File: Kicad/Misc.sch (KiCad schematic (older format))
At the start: 34 parts, among them IC1 DS1233-10+, J1 Data Bus Pin Header, J2 Address Bus Pin Header, J3 uSeq Pin Header, SW1 SW_Push, U21 74HCT139, U26 ECS-100AX-035

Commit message: Added the equ pseudo-op. Rearranged the PCB layout.
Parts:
- removed C24: 0.1uF, Capacitor_SMD:C_0603_1608Metric_Pad1.05x0.95mm_HandSolder, symbol Device:C_Small
- added J4: Control Lines Pin Header, Connector_PinSocket_2.54mm:PinSocket_1x18_P2.54mm_Vertical, symbol Connector:Conn_01x18_Female
- added J5: Clock Pin Header, Connector_PinSocket_2.54mm:PinSocket_1x02_P2.54mm_Vertical, symbol Connector:Conn_01x02_Female
- U21: footprint Package_SO:SOIC-16W_5.3x10.2mm_P1.27mm -> Package_SO:SOIC-16_3.9x9.9mm_P1.27mm
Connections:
- net Clk: now also J5.1 (Pin_1)
- net GND: now also J4.1 (Pin_1), J5.2 (Pin_2)
- net VCC: now also J1.9 (Pin_9), J2.17 (Pin_17), J3.5 (Pin_5), J4.2 (Pin_2)
- new net ALUop0: J4.3 (Pin_3)
- new net ALUop1: J4.4 (Pin_4)
- new net ALUop2: J4.5 (Pin_5)
- new net ALUop3: J4.6 (Pin_6)
- new net AbWr0: J4.10 (Pin_10)
- new net AbWr1: J4.11 (Pin_11)
- new net DbRd0: J4.12 (Pin_12)
- new net DbRd1: J4.13 (Pin_13)
- new net DbRd2: J4.14 (Pin_14)
- new net DbRd3: J4.15 (Pin_15)
- new net DbWr0: J4.7 (Pin_7)
- new net DbWr1: J4.8 (Pin_8)
- new net DbWr2: J4.9 (Pin_9)
- new net StkOp0: J4.16 (Pin_16)
- new net StkOp1: J4.17 (Pin_17)
- new net ~uSreset: J4.18 (Pin_18)
- no-connect marks 4 -> 1
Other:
- moved on the sheet: C25, C26, C27, IC1

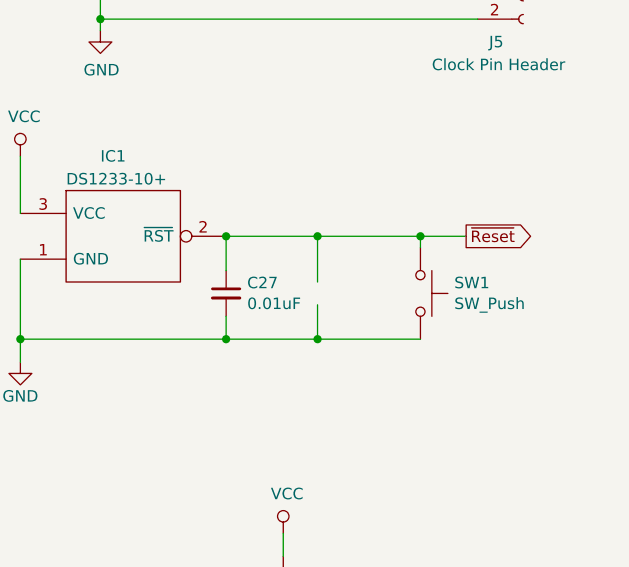
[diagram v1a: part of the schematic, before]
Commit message: Lots of changes.
I found a few wiring mistakes in the schematic and fixed them up.
I added microcode instructions to allow B to be copied out to A,
to the UART and to memory. I added a lot of `mem = mem op B`
instructions. I added some examples to test the above. I redid the
PCB layout and added copper pours.
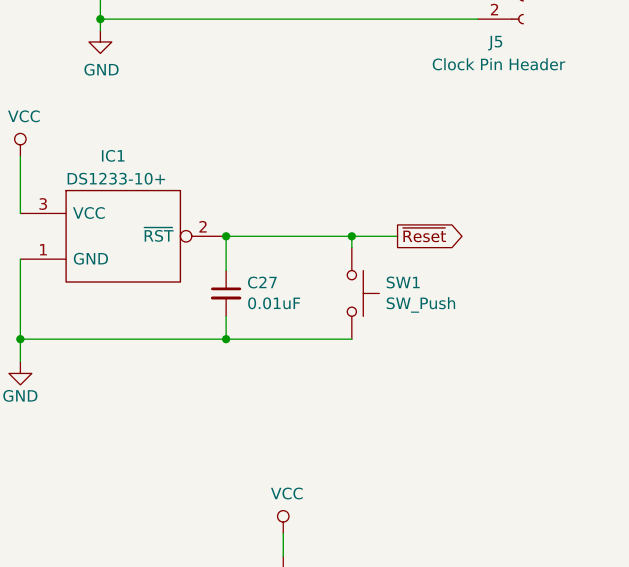
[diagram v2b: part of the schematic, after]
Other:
- moved on the sheet: SW1
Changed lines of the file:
@@
 encoding utf-8
 Sheet 3 5
-Title ""
-Date ""
+Title "FISC TTL CPU"
+Date "2020-05-21"
 Rev ""
 Comp ""
@@
 Text GLabel 10250 2250 2    50   Output ~ 0
 Clk
-Text GLabel 10200 3500 2    50   Output ~ 0
+Text GLabel 9900 3500 2    50   Output ~ 0
 ~Reset
 $Comp
@@
 L Switch:SW_Push SW1
 U 1 1 5EC0EA9A
-P 10000 3750
-F 0 "SW1" V 9954 3898 50  0000 L CNN
-F 1 "SW_Push" V 10045 3898 50  0000 L CNN
-F 2 "Button_Switch_THT:Push_E-Switch_KS01Q01" H 10000 3950 50  0001 C CNN
-F 3 "" H 10000 3950 50  0001 C CNN
-F 4 "Reset button" H 10000 3750 50  0001 C CNN "Description"
-	1    10000 3750
+P 9700 3750
+F 0 "SW1" V 9654 3898 50  0000 L CNN
+F 1 "SW_Push" V 9745 3898 50  0000 L CNN
+F 2 "Button_Switch_THT:Push_E-Switch_KS01Q01" H 9700 3950 50  0001 C CNN
+F 3 "" H 9700 3950 50  0001 C CNN
+F 4 "Reset button" H 9700 3750 50  0001 C CNN "Description"
+	1    9700 3750
 	0    1    1    0
 $EndComp
 Wire Wire Line
-	10000 3550 10000 3500
-Connection ~ 10000 3500
-Wire Wire Line
-	10000 3500 10200 3500
+	9700 3550 9700 3500
+Connection ~ 9700 3500
+Wire Wire Line
+	9700 3500 9900 3500
 Wire Wire Line
 	9150 3650 9150 3500
@@
 $EndComp
 Wire Wire Line
-	9150 3500 9550 3500
-Connection ~ 9150 3500
-Wire Wire Line
-	9150 3950 9550 3950
-Connection ~ 9150 3950
-Wire Wire Line
-	9550 3700 9550 3500
-Connection ~ 9550 3500
-Wire Wire Line
-	9550 3500 10000 3500
-Wire Wire Line
-	9550 3800 9550 3950
-Connection ~ 9550 3950
-Wire Wire Line
-	9550 3950 10000 3950
-Wire Wire Line
 	2400 2850 2650 2850
 Wire Wire Line
@@
 Wire Wire Line
 	5950 6100 5950 6050
+Wire Wire Line
+	9150 3500 9700 3500
+Wire Wire Line
+	9150 3950 9700 3950
+Connection ~ 9150 3500
+Connection ~ 9150 3950
 Wire Bus Line
 	3600 4650 3600 5550
